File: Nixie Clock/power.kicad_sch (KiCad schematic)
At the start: 35 parts, among them J2 USB_C_Receptacle_USB2.0_14P, Q20 IRF740, U2 TPD4E02B04DQA, U3 AMS1117-3.3, U7 MAX1771xSA

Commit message: PCB routed
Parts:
- removed C22: 200uF/16V, symbol Device:C
- removed R58: 1M, symbol Device:R
- added C45: 220uF/16V, Capacitor_SMD:CP_Elec_10x10, symbol Device:C_Polarized
- C42: renamed from C23; footprint (none) -> Capacitor_SMD:CP_Elec_6.3x7.7
- C43: renamed from C26; footprint (none) -> Capacitor_SMD:C_0603_1608Metric
- C44: renamed from C28; footprint (none) -> Capacitor_SMD:C_0603_1608Metric
- C46: renamed from C24; footprint (none) -> Capacitor_SMD:C_0603_1608Metric
- C47: renamed from C25; footprint (none) -> Capacitor_SMD:C_0603_1608Metric
- C48: renamed from C29; footprint (none) -> Capacitor_SMD:CP_Elec_8x10.5
- C49: renamed from C27; footprint (none) -> Capacitor_SMD:C_0603_1608Metric
- C50: renamed from C32; footprint (none) -> Capacitor_SMD:C_0603_1608Metric
- C51: renamed from C30; footprint (none) -> Capacitor_SMD:CP_Elec_10x10.5
- C52: renamed from C31; footprint (none) -> Capacitor_SMD:CP_Elec_10x10.5
- C53: renamed from C33; value 0.1uF -> 100nF; footprint (none) -> Capacitor_SMD:C_0603_1608Metric
- D20: renamed from D24; footprint (none) -> Diode_THT:D_DO-201AD_P12.70mm_Horizontal
- D21: renamed from D25; footprint (none) -> LED_SMD:LED_0201_0603Metric
- D22: renamed from D27; footprint (none) -> Diode_SMD:D_SMB
- D23: renamed from D26; footprint (none) -> Diode_THT:D_DO-201AD_P12.70mm_Horizontal
- J6: renamed from J2; footprint (none) -> Connector_USB:USB_C_Receptacle_G-Switch_GT-USB-7051x
- L1: renamed from L5; footprint (none) -> Inductor_SMD:L_12x12mm_H8mm
- L2: renamed from L3; value 150uH -> 100uH; footprint (none) -> Inductor_SMD:L_12x12mm_H8mm
- Q3: renamed from Q20; footprint Package_TO_SOT_THT:TO-220-3_Vertical -> Package_TO_SOT_THT:TO-220-3_Horizontal_TabUp
- R34: renamed from R59; footprint (none) -> Resistor_SMD:R_0603_1608Metric
- R35: renamed from R60; footprint (none) -> Resistor_SMD:R_0603_1608Metric
- R36: renamed from R61; footprint (none) -> Resistor_SMD:R_0603_1608Metric
- R37: renamed from R63; footprint (none) -> Resistor_SMD:R_0603_1608Metric
- R38: renamed from R62; footprint (none) -> Resistor_SMD:R_0603_1608Metric
- R39: renamed from R66; footprint (none) -> Resistor_SMD:R_0603_1608Metric
- R40: renamed from R67; footprint (none) -> Resistor_SMD:R_0603_1608Metric
- R41: renamed from R64; footprint (none) -> Resistor_SMD:R_0603_1608Metric
- R42: renamed from R65; footprint (none) -> Resistor_SMD:R_0603_1608Metric
- RV1: renamed from RV2; footprint (none) -> Potentiometer_THT:Potentiometer_Bourns_3296W_Vertical
- renumbered U2 to U10, U7 to U11, U3 to U12, VR2 to VR1
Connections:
- net +5V: now also C45.1
- net GND: now also J6.S1 (SHIELD), C45.2
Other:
- title: (none) -> Nixie Clock

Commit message: Rev2.1 depopulated R30 and R31 pullup resistors
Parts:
- C50: footprint Capacitor_SMD:C_0603_1608Metric -> Capacitor_SMD:C_1206_3216Metric

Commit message: change R37 and R39 to higher rated resistors
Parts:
- R37: footprint Resistor_SMD:R_0603_1608Metric -> Resistor_SMD:R_0805_2012Metric
- R39: footprint Resistor_SMD:R_0603_1608Metric -> Resistor_SMD:R_2512_6332Metric
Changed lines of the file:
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@@
 			)
 		)
-		(property "Footprint" "Resistor_SMD:R_0603_1608Metric"
+		(property "Footprint" "Resistor_SMD:R_2512_6332Metric"
 			(at 131.572 132.08 90)
 			(hide yes)
@@
 			)
 		)
-		(property "Footprint" "Resistor_SMD:R_0603_1608Metric"
+		(property "Footprint" "Resistor_SMD:R_0805_2012Metric"
 			(at 102.362 153.67 90)
 			(hide yes)

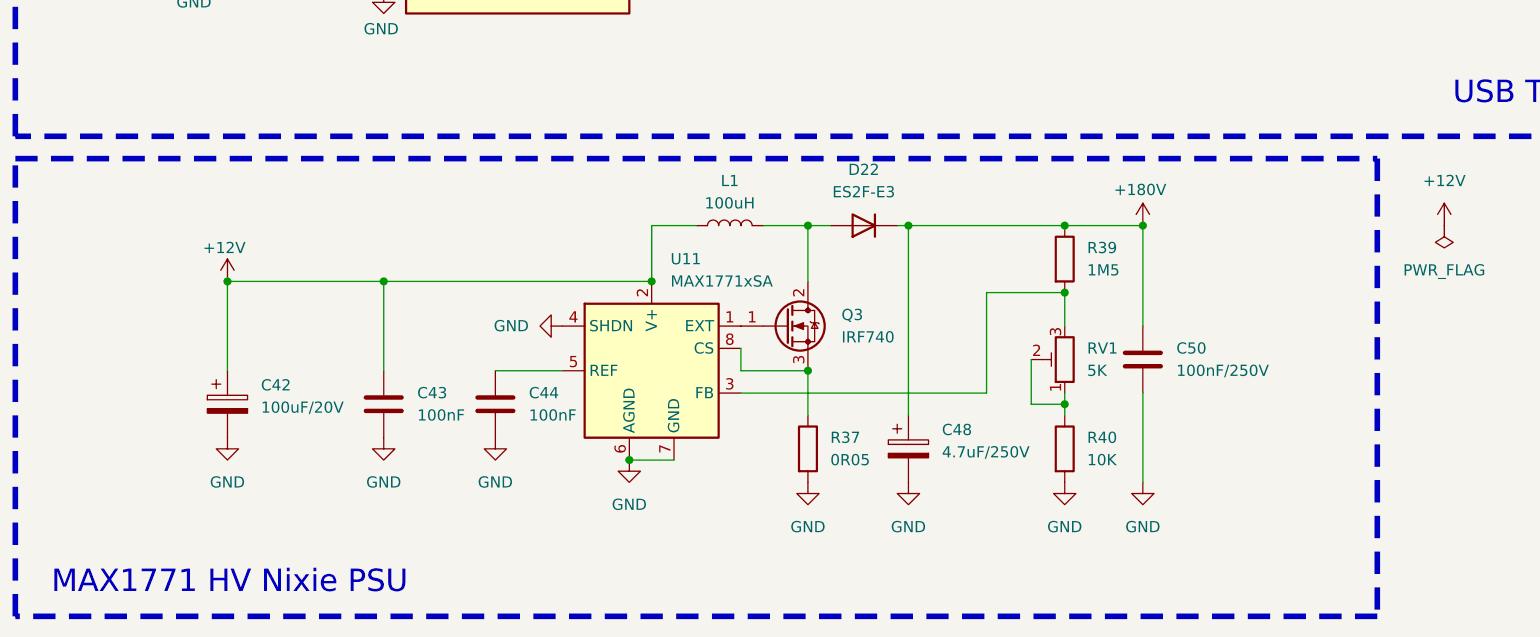
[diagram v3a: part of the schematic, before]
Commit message: Add capacitor across R39 for filtering
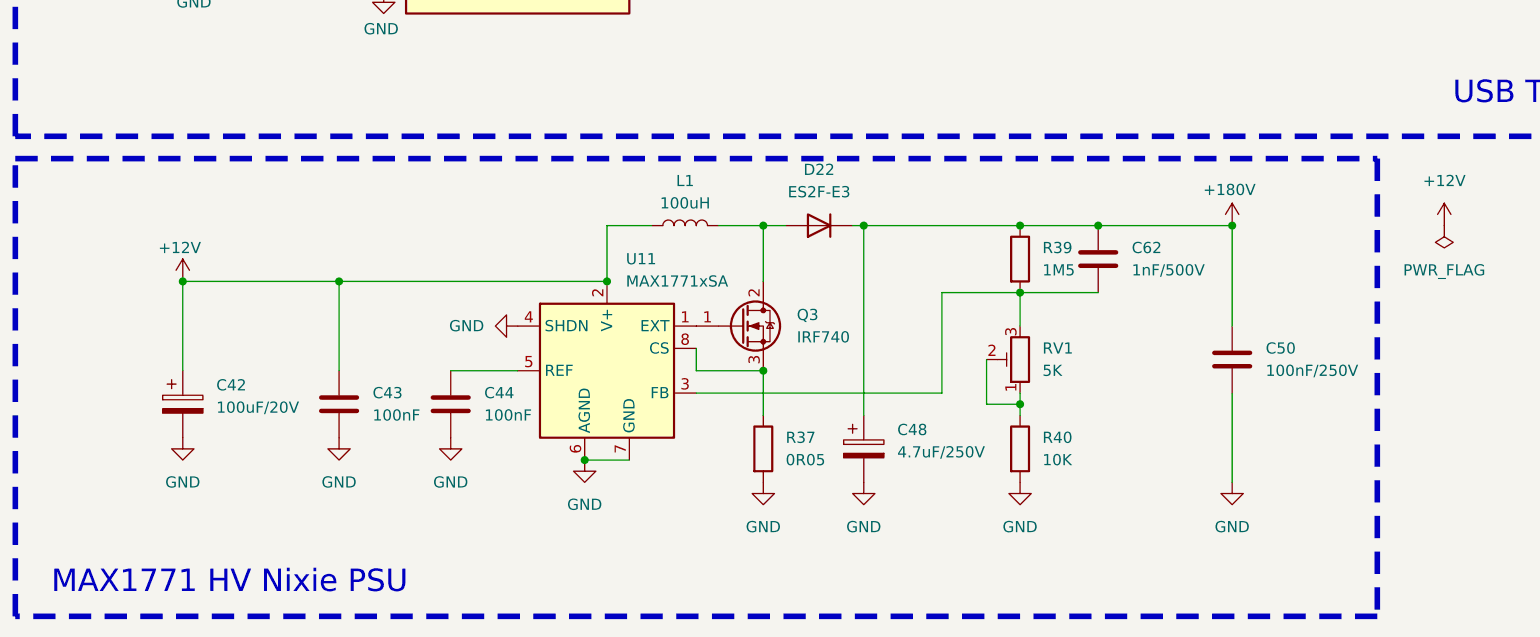
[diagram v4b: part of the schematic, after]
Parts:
- added C62: 1nF/500V, Capacitor_SMD:C_1206_3216Metric, symbol Device:C
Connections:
- net +180V: now also C62.1
- net at R39.2, RV1.3, U11.3 (FB): now also C62.2
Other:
- moved on the sheet: C42, C43, C44, C48, C50, D22, L1, Q3, R37, R39, R40, RV1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
